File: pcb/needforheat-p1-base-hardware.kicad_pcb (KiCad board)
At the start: 2 copper layers, 51 x 36 mm, 18 parts, among them IC1 74HC14D,653, J1 Conn_02x08_Counter_Clockwise, J2 RJ12, J3 RJ12, Q1 MMBT3904, Q2 MMBT5401, SW1 DSHP03TSGER, U1 SFH6206-2T

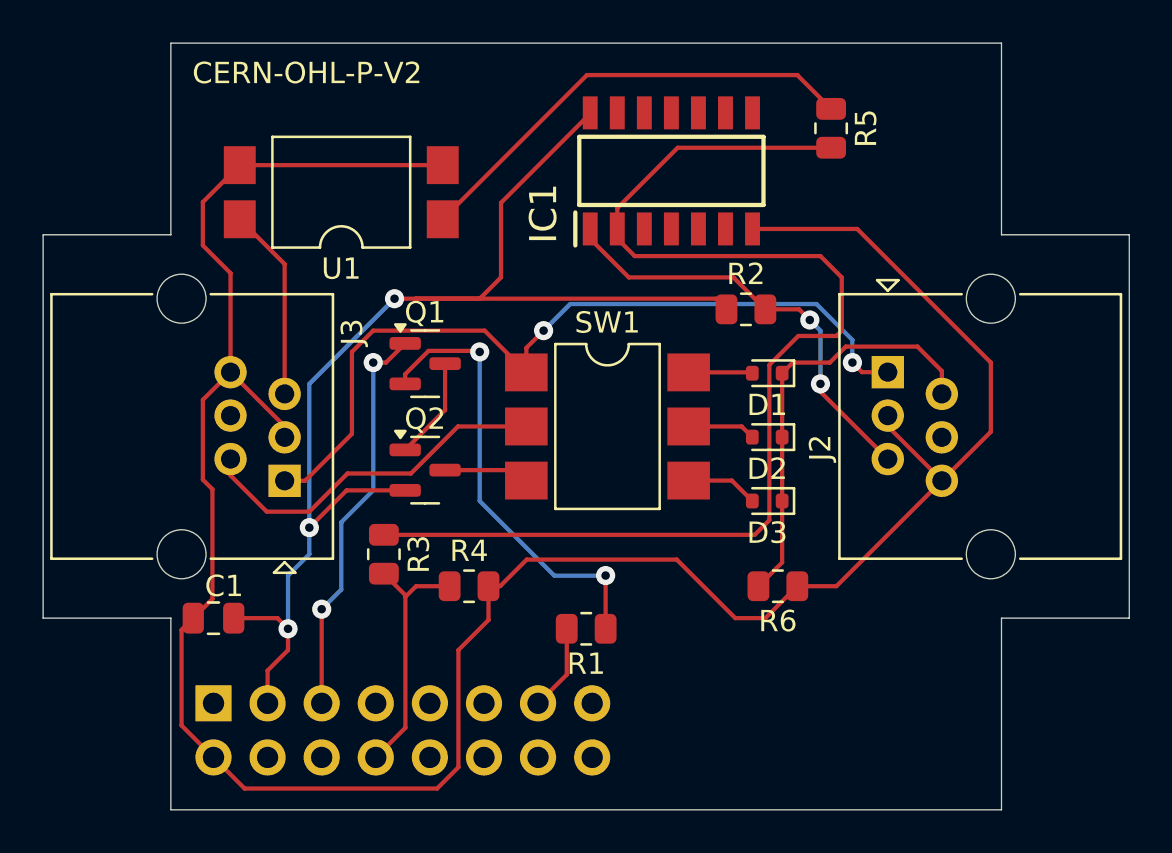
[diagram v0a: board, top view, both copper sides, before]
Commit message: updated the pcb files to p1-base v2.4
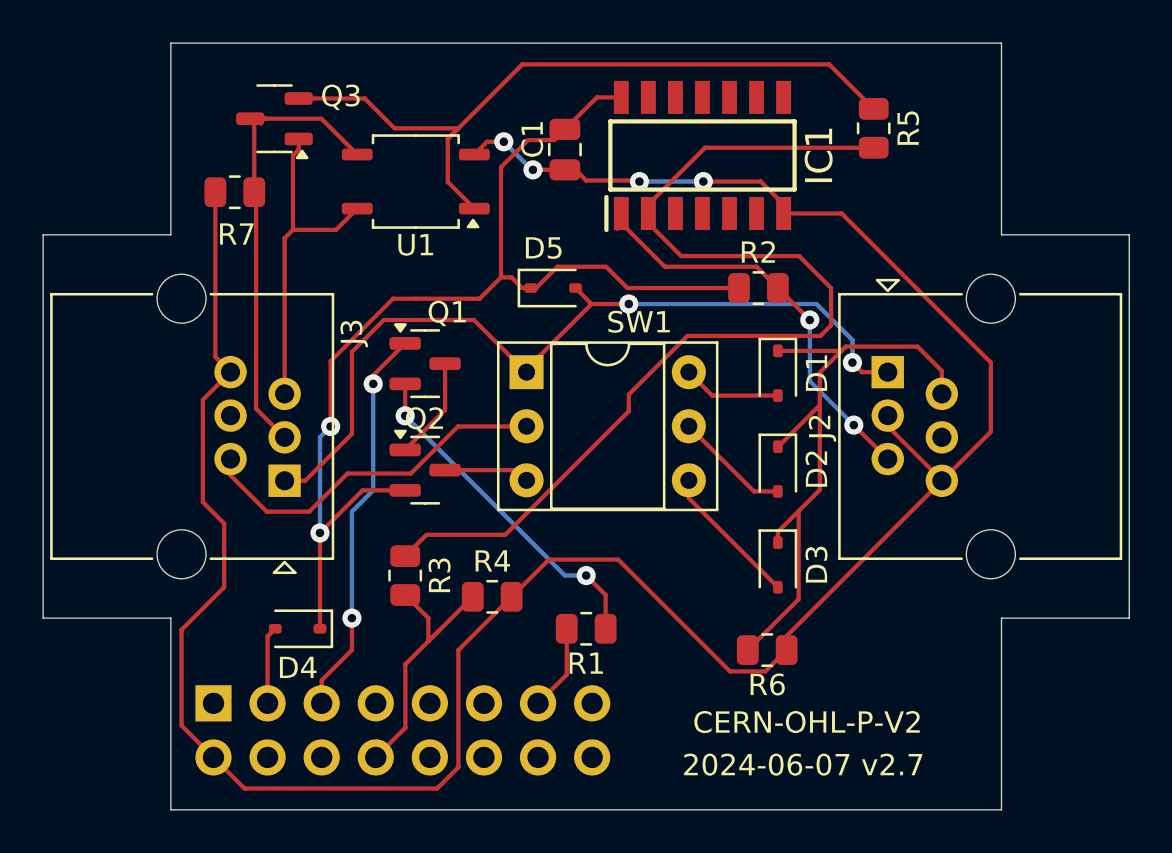
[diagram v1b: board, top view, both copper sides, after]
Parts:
- added D4: 1N5819WS, Diode_SMD:D_SOD-323, F.Cu at (88.5, 76.5)
- added D5: 1N5819WS, Diode_SMD:D_SOD-323, F.Cu at (100.5, 60.5)
- added Q3: TBC847_E_20160525, Package_TO_SOT_SMD:SOT-23-3, F.Cu at (87.4, 52.5)
- added R7: 0, Resistor_SMD:R_0805_2012Metric, F.Cu at (85.5, 56.0)
- D1, D2, D3: value SS14 -> 1N5819WS; footprint Diode_SMD:D_SOD-523 -> Diode_SMD:D_SOD-323
- SW1: value DSHP03TSGER -> KF1001-03P-R0-GL-DFT-01B; footprint Package_DIP:SMDIP-6_W7.62mm -> Package_DIP:DIP-6_W7.62mm_Socket
- U1: value SFH6206-2T -> EL357N-G; footprint Package_DIP:SMDIP-4_W9.53mm_Clearance8mm -> Package_SO:SOP-4_3.8x4.1mm_P2.54mm
- moved C1 27.5 mm to (101.0, 54.0), turned to -90 degrees
- moved SW1 4.58 mm to (99.2, 64.5)
- moved U1 3.54 mm to (94.0, 55.5)
- moved D3 3.04 mm to (111.0, 73.5), turned to -90 degrees
- moved R6 3.04 mm to (110.5, 77.5)
- moved R5 2.00 mm to (115.5, 53.0)
- moved IC1 1.63 mm to (107.5, 54.3)
- moved D2 1.58 mm to (111.0, 69.0), turned to -90 degrees
- moved R3 1.41 mm to (93.5, 74.0)
- moved R4 1.20 mm to (97.6, 75.0)
- moved R2 1.16 mm to (110.1, 60.5)
- moved D1 0.50 mm to (111.0, 64.5), turned to -90 degrees
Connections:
- C1 pad 2: EXT_DATA_GND -> GND
- IC1 pad 7: EXT_DATA_GND -> GND
- J1 pad 5VOUT: VCC -> Net-(D4-A)
- J1 pad GND: EXT_DATA_GND -> GND
- J2 pad 3: EXT_DATA_GND -> GND
- J2 pad 6: EXT_DATA_GND -> GND
- J3 pad 6: EXT_DATA_GND -> GND
- R4 pad 2: EXT_DATA_GND -> GND
- R6 pad 1: EXT_DATA_GND -> GND
- U1 pad 2: EXT_DATA_GND -> GND
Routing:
- net GND: track 0.00 -> 118.7 mm, vias 0 -> 4
- net EXT_DATA_GND: track 117.3 -> 22.4 mm
- net Net-(Q3-B): track 21.7 -> 34.9 mm
- net METER_DATA_REQ: track 20.0 -> 30.1 mm
- net VCC: track 59.0 -> 51.6 mm, vias 3 -> 2
- net Net-(IC1-1Y): track 56.2 -> 49.1 mm
- net EXT_DATA: track 9.07 -> 15.7 mm
- net Net-(Q1-E): track 21.3 -> 16.0 mm
- net Net-(D4-A): track 0.00 -> 3.65 mm
- net Net-(D3-A): track 3.39 -> 6.75 mm
- net Net-(D1-A): track 3.01 -> 5.27 mm
- net Net-(D2-A): track 3.20 -> 5.45 mm
- net 5V_METER: track 38.3 -> 39.1 mm
- net Reader_IN: track 11.9 -> 12.8 mm
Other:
- board text added: "2024-06-07 v2.7"
